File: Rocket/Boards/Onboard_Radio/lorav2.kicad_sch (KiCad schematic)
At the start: 31 parts, among them J6 RFIO SMA, U2 SX1262, U3 PE4259 RF Switch, Y1 32.000MHz

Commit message: can bus updeated
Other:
- title: (none) -> Radio IC
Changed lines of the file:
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@@
 	(generator_version "10.0")
 	(paper "A4")
+	(title_block
+		(title "Radio IC")
+		(date "2026-05-28")
+		(rev "A")
+	)
 	(rectangle
 		(start 15.24 24.13)

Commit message: post narottam meetup
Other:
- note added: "stm32wl"
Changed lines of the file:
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@@
+		)
+	)
+	(text "stm32wl"
+		(exclude_from_sim no)
+		(at 23.876 183.642 0)
+		(effects
+			(font
+				(size 1.27 1.27)
+			)
 		)
 	)

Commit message: radio ic board planes joined, pcb made smaller, need to add cantraces before review
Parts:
- J6: footprint Library:JOHNSON_142-0701-841 -> Library:SMA-KE-16.5A_EdgeMount
- Y1: footprint (none) -> Crystal:Crystal_SMD_Abracon_ABM8G-4Pin_3.2x2.5mm; MPN CS06465-32M -> ABM8-32.000MHZ-B2-T; Manufacturer NDK (NIHON DEMPA KOGYO CO., LTD) -> Abracon LLC
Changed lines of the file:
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@@
 		)
 	)
+	(rule_area
+		(exclude_from_sim no)
+		(in_bom yes)
+		(on_board yes)
+		(dnp no)
+		(polyline
+			(pts
+				(xy 15.24 21.59) (xy 270.51 21.59) (xy 283.21 34.29) (xy 283.21 135.89) (xy 270.51 148.59) (xy 25.4 148.59)
+				(xy 20.32 143.51) (xy 20.32 26.67)
+			)
+			(stroke
+				(width 0)
+				(type dash)
+			)
+			(fill
+				(type none)
+			)
+		)
+	)
+	(netclass_flag ""
+		(length 2.54)
+		(shape round)
+		(at 111.76 21.59 0)
+		(fields_autoplaced yes)
+		(effects
+			(font
+				(size 1.27 1.27)
+			)
+			(justify left bottom)
+		)
+		(property "Net Class" "RF_50Ohm"
+			(at 112.4585 19.05 0)
+			(show_name no)
+			(do_not_autoplace no)
+			(effects
+				(font
+					(size 1.27 1.27)
+				)
+				(justify left)
+			)
+		)
+		(property "Component Class" ""
+			(at 105.41 66.04 0)
+			(show_name no)
+			(do_not_autoplace no)
+			(effects
+				(font
+					(size 1.27 1.27)
+					(italic yes)
+				)
+			)
+		)
+	)
 	(symbol
 		(lib_id "power:GND")
@@
 			)
 		)
-		(property "Footprint" ""
+		(property "Footprint" "Crystal:Crystal_SMD_Abracon_ABM8G-4Pin_3.2x2.5mm"
 			(at 27.94 64.77 0)
 			(hide yes)
@@
 			)
 		)
-		(property "MPN" "CS06465-32M"
+		(property "MPN" "ABM8-32.000MHZ-B2-T"
 			(at 27.94 64.77 0)
 			(hide yes)
@@
 			)
 		)
-		(property "Manufacturer" "NDK (NIHON DEMPA KOGYO CO., LTD)"
+		(property "Manufacturer" "Abracon LLC"
 			(at 27.94 64.77 0)
 			(hide yes)
@@
 			)
 		)
-		(property "Footprint" "Library:JOHNSON_142-0701-841"
+		(property "Footprint" "Library:SMA-KE-16.5A_EdgeMount"
 			(at 270.51 100.33 0)
 			(hide yes)

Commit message: schematic ready for review
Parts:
- C1: MPN GRM155R71C473KA01D -> GJM1555C1H470JB01D; Voltage 16V -> 50V
- C13, C3: now not fitted; now left out of the parts list
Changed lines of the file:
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@@
 		(polyline
 			(pts
-				(xy 15.24 21.59) (xy 270.51 21.59) (xy 283.21 34.29) (xy 283.21 135.89) (xy 270.51 148.59) (xy 25.4 148.59)
-				(xy 20.32 143.51) (xy 20.32 26.67)
+				(xy 16.51 21.59) (xy 262.89 21.59) (xy 275.59 34.29) (xy 275.59 135.89) (xy 262.89 148.59) (xy 17.78 148.59)
+				(xy 12.7 143.51) (xy 12.7 26.67)
 			)
 			(stroke
@@
 			)
 		)
-		(property "Datasheet" "https://search.murata.co.jp/Ceramy/image/img/A01X/G101/ENG/GRM155R71C473KA01-01.pdf"
+		(property "Datasheet" "https://search.murata.co.jp/Ceramy/image/img/A01X/G101/ENG/GJM1555C1H470JB01-01.pdf"
 			(at 100.33 82.55 0)
 			(hide yes)
@@
 			)
 		)
-		(property "Description" "0.047 µF ±10% 16V Ceramic Capacitor X7R 0402 (1005 Metric)"
+		(property "Description" "47 pF ±5% 50V Ceramic Capacitor C0G, NP0 0402 (1005 Metric)"
 			(at 100.33 82.55 0)
 			(hide yes)
@@
 			)
 		)
-		(property "MPN" "GRM155R71C473KA01D "
+		(property "MPN" "GJM1555C1H470JB01D "
 			(at 100.33 82.55 0)
 			(hide yes)
@@
 			)
 		)
-		(property "Voltage" "16V"
+		(property "Voltage" "50V"
 			(at 100.33 82.55 0)
 			(hide yes)
@@
 		(body_style 1)
 		(exclude_from_sim no)
-		(in_bom yes)
+		(in_bom no)
 		(on_board yes)
 		(in_pos_files yes)
-		(dnp no)
+		(dnp yes)
 		(property "Reference" "C3"
 			(at 120.142 94.488 0)
@@
 		(body_style 1)
 		(exclude_from_sim no)
-		(in_bom yes)
+		(in_bom no)
 		(on_board yes)
 		(in_pos_files yes)
-		(dnp no)
+		(dnp yes)
 		(property "Reference" "C13"
 			(at 122.682 114.808 0)

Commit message: everything minus trace impedance and via stictching
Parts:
- U3: footprint Package_TO_SOT_SMD:Vishay_PowerPAK_SC70-6L_Dual -> Package_TO_SOT_SMD:SOT-363_SC-70-6
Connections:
- net VDD_RADIO renamed +3V3A

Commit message: rf traces updated, need to workout board net class
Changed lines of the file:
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@@
 	(wire
 		(pts
-			(xy 52.07 115.57) (xy 57.15 115.57)
+			(xy 25.4 115.57) (xy 57.15 115.57)
 		)
 		(stroke
@@
 	(wire
 		(pts
-			(xy 52.07 110.49) (xy 57.15 110.49)
+			(xy 25.4 110.49) (xy 57.15 110.49)
 		)
 		(stroke
@@
 	(wire
 		(pts
-			(xy 52.07 113.03) (xy 57.15 113.03)
-		)
-		(stroke
-			(width 0)
-			(type default)
-		)
-	)
-	(wire
-		(pts
-			(xy 52.07 107.95) (xy 57.15 107.95)
+			(xy 25.4 113.03) (xy 57.15 113.03)
+		)
+		(stroke
+			(width 0)
+			(type default)
+		)
+	)
+	(wire
+		(pts
+			(xy 25.4 107.95) (xy 57.15 107.95)
 		)
 		(stroke
@@
 	(hierarchical_label "MOSI"
 		(shape input)
-		(at 52.07 113.03 180)
+		(at 25.4 113.03 180)
 		(effects
 			(font
@@
 	(hierarchical_label "NSS"
 		(shape input)
-		(at 52.07 115.57 180)
+		(at 25.4 115.57 180)
 		(effects
 			(font
@@
 	(hierarchical_label "SCK"
 		(shape input)
-		(at 52.07 107.95 180)
+		(at 25.4 107.95 180)
 		(effects
 			(font
@@
 	(hierarchical_label "MISO"
 		(shape input)
-		(at 52.07 110.49 180)
+		(at 25.4 110.49 180)
 		(effects
 			(font
@@
 	(hierarchical_label "BUSY"
 		(shape input)
-		(at 90.17 115.57 0)
-		(effects
-			(font
-				(size 1.27 1.27)
-			)
-			(justify left)
+		(at 90.17 115.57 270)
+		(effects
+			(font
+				(size 1.27 1.27)
+			)
+			(justify right)
 		)
 	)
@@
 		(polyline
 			(pts
-				(xy 16.51 21.59) (xy 262.89 21.59) (xy 275.59 34.29) (xy 275.59 135.89) (xy 262.89 148.59) (xy 17.78 148.59)
-				(xy 12.7 143.51) (xy 12.7 26.67)
+				(xy 100.33 38.1) (xy 274.32 38.1) (xy 280.67 43.18) (xy 280.67 125.73) (xy 275.59 130.81) (xy 99.06 130.81)
+				(xy 93.98 126.365) (xy 93.98 43.815)
 			)
 			(stroke
@@
 		(length 2.54)
 		(shape round)
-		(at 111.76 21.59 0)
-		(fields_autoplaced yes)
+		(at 115.57 38.1 0)
 		(effects
 			(font
@@
 		)
 		(property "Net Class" "RF_50Ohm"
-			(at 112.4585 19.05 0)
+			(at 116.2685 35.56 0)
 			(show_name no)
 			(do_not_autoplace no)
@@
 		)
 		(property "Component Class" ""
-			(at 105.41 66.04 0)
+			(at 109.22 82.55 0)
 			(show_name no)
 			(do_not_autoplace no)

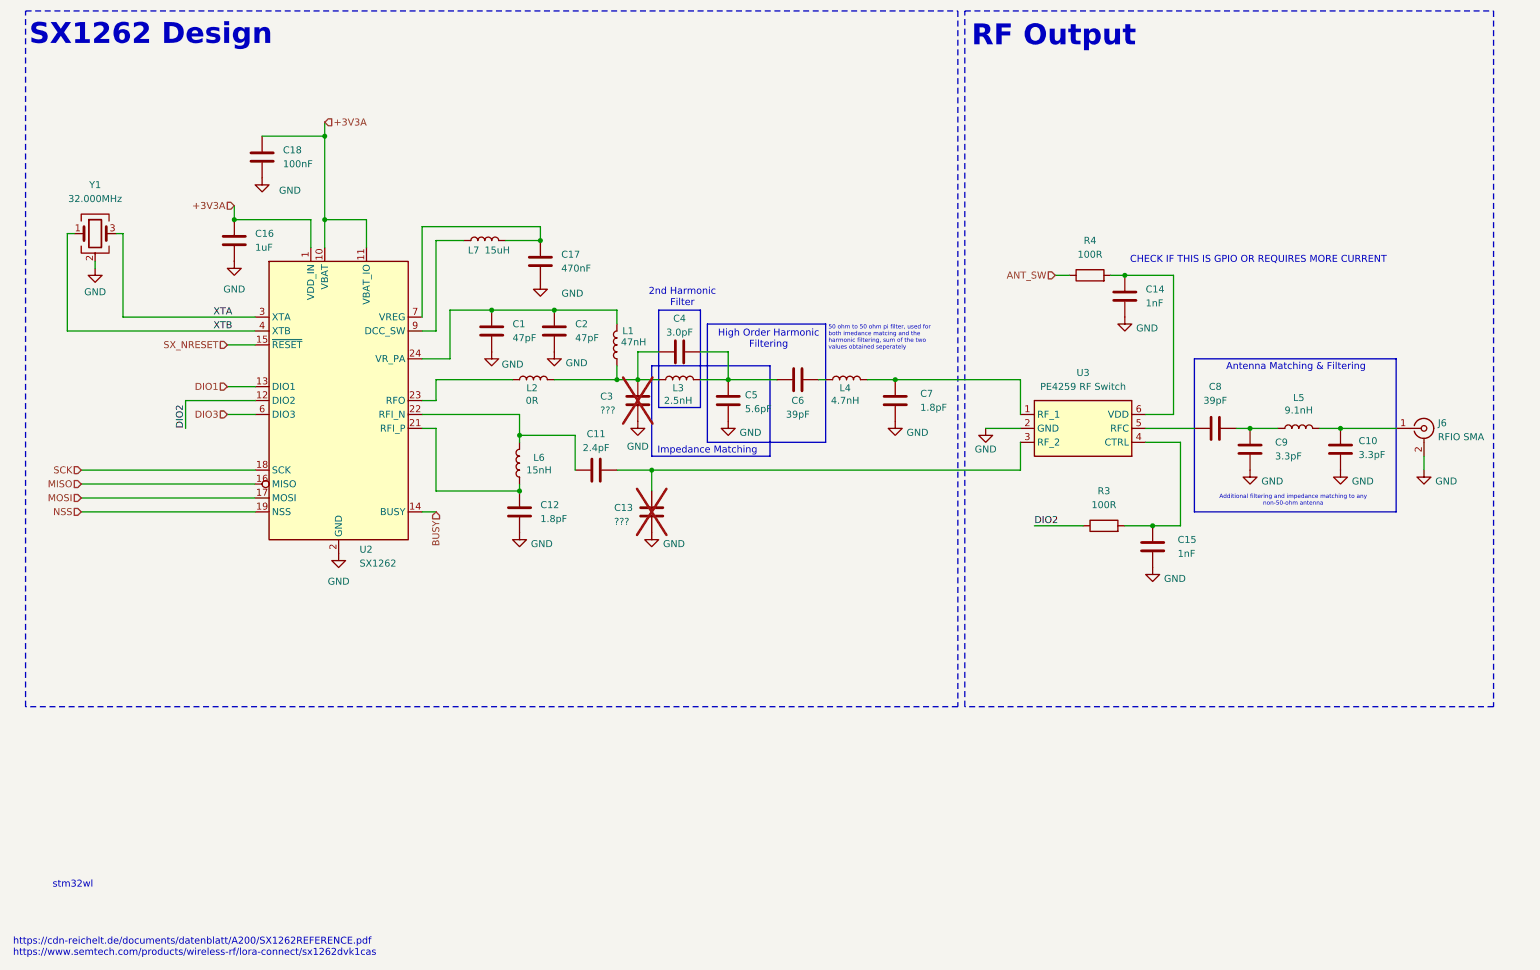
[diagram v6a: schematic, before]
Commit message: via fencing done, need via stiching
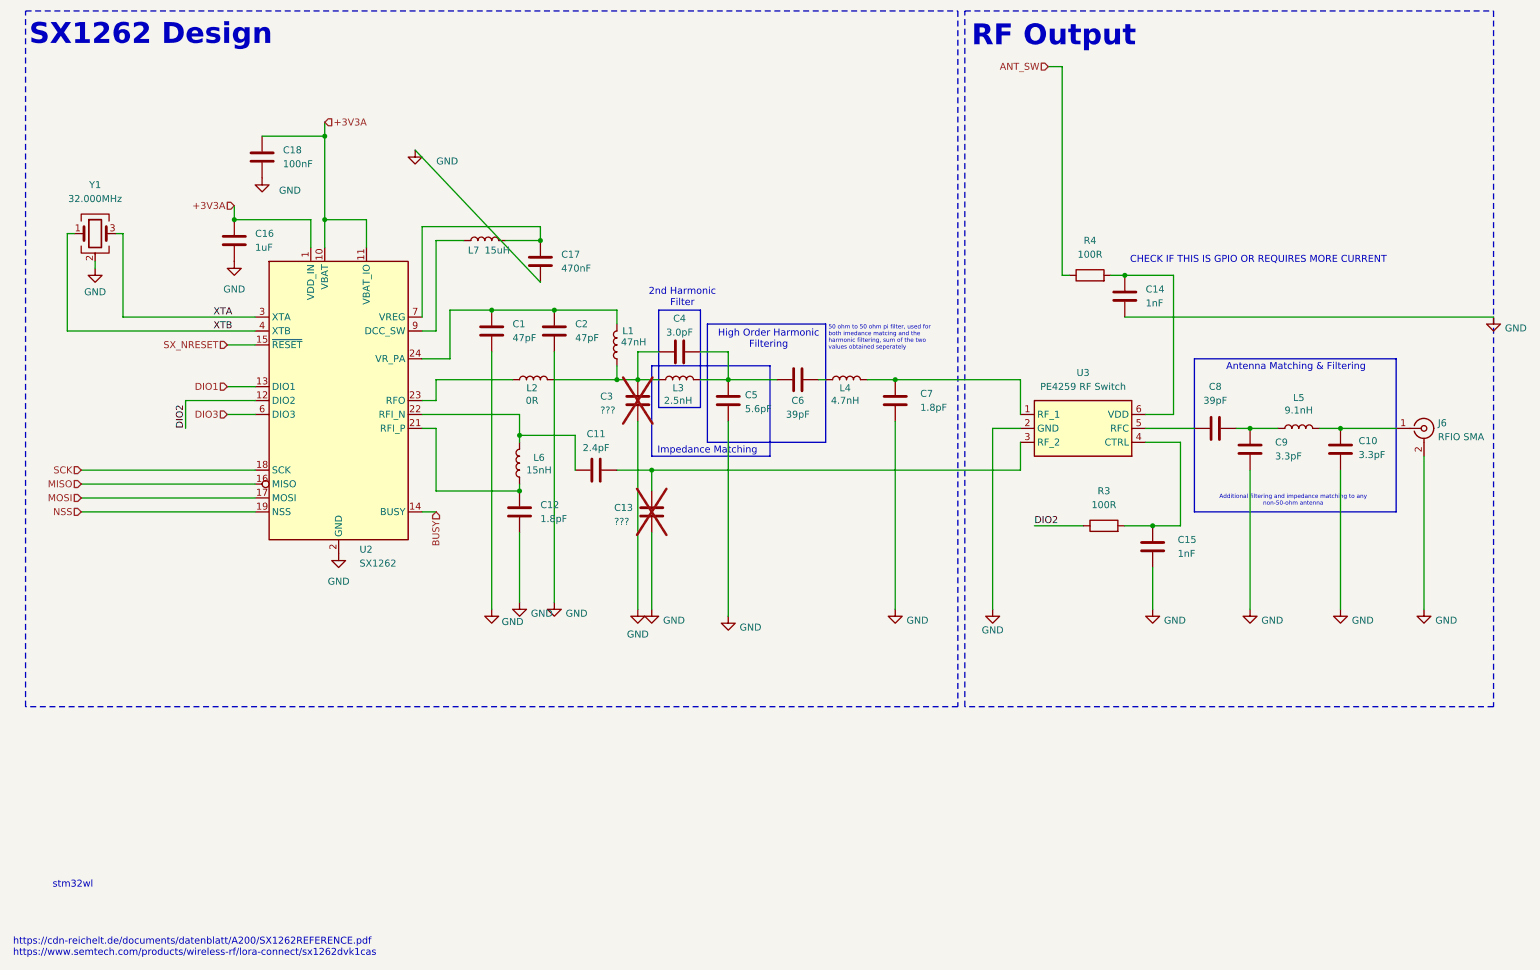
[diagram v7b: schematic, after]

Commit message: needs pcb and schematic review
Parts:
- C1, C2: LCSC Part # (none) -> C161322
- C10, C9: LCSC Part # (none) -> C76906
- C11: LCSC Part # (none) -> C88888
- C12, C7: LCSC Part # (none) -> C76902
- C14, C15: LCSC Part # (none) -> C162197
- C16: LCSC Part # (none) -> C77006
- C17: LCSC Part # (none) -> C88946
- C18: LCSC Part # (none) -> C77020
- C4: LCSC Part # (none) -> C88891
- C5: LCSC Part # (none) -> C88895
- C6, C8: LCSC Part # (none) -> C426038
- J6: LCSC Part # (none) -> C3173357
- L1: LCSC Part # (none) -> C192855
- L2: LCSC Part # (none) -> C190119
- L3: LCSC Part # (none) -> C703121
- L4: LCSC Part # (none) -> C167480
- L5: LCSC Part # (none) -> C337956
- L6: LCSC Part # (none) -> C91621
- L7: LCSC Part # (none) -> C383402
- R3, R4: LCSC Part # (none) -> C82865
- U2: LCSC Part # (none) -> C191341
- U3: LCSC Part # (none) -> C470892
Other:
- note removed: "CHECK IF THIS IS GPIO OR REQUIRES MORE CURRENT"
